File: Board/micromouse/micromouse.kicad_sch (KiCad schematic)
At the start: 51 parts, among them J1 Conn_01x02_Pin, J2 Conn_02x03_Odd_Even, J4 Conn_01x06_Pin, J5 Conn_01x06_Pin, M1 Motor_DC, M2 Motor_DC, Q1 DMN63D8L-7, Q7 GSFC02A05, SW1 AYZ0102AGRLC, SW2 NANOT 100 AS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

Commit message: レビュー対応
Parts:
- D10, D11, D12, D13: footprint LED_SMD:LED_0603_1608Metric -> LED_SMD:LED_0402_1005Metric
- J1: footprint Connector_JST:JST_PH_B2B-PH-SM4-TB_1x02-1MP_P2.00mm_Vertical -> Connector_JST:JST_PH_B2B-PH-K_1x02_P2.00mm_Vertical
- R24, R25, R26, R27, R4: value 1k -> 3.3k
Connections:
- net +3.3V: now also R1.2, R2.2, R33.1; no longer SW4.2
- net GND: now also R23.1, SW4.1; no longer Q7.1 (G), R33.2
- net NRST: now also R33.2, SW4.2; no longer R33.1, SW4.1
- net at R3.2, SW1.1 (A): now also Q7.1 (G)
- no-connect marks 22 -> 19
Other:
- moved on the sheet: R1, R2, R33, SW1

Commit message: ボタン位置修正
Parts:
- D1: footprint LED_SMD:LED_0603_1608Metric -> LED_SMD:LED_0402_1005Metric_Pad0.77x0.64mm_HandSolder
- D10, D11, D12, D13: footprint LED_SMD:LED_0402_1005Metric -> LED_SMD:LED_0402_1005Metric_Pad0.77x0.64mm_HandSolder
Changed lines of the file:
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@@
       (effects (font (size 1.27 1.27)) (justify right))
     )
-    (property "Footprint" "LED_SMD:LED_0603_1608Metric" (at 114.3 31.75 0)
+    (property "Footprint" "LED_SMD:LED_0402_1005Metric_Pad0.77x0.64mm_HandSolder" (at 114.3 31.75 0)
       (effects (font (size 1.27 1.27)) hide)
     )
@@
       (effects (font (size 1.27 1.27)))
     )
-    (property "Footprint" "LED_SMD:LED_0402_1005Metric" (at 267.97 73.66 0)
+    (property "Footprint" "LED_SMD:LED_0402_1005Metric_Pad0.77x0.64mm_HandSolder" (at 267.97 73.66 0)
       (effects (font (size 1.27 1.27)) hide)
     )
@@
       (effects (font (size 1.27 1.27)))
     )
-    (property "Footprint" "LED_SMD:LED_0402_1005Metric" (at 267.97 88.9 0)
+    (property "Footprint" "LED_SMD:LED_0402_1005Metric_Pad0.77x0.64mm_HandSolder" (at 267.97 88.9 0)
       (effects (font (size 1.27 1.27)) hide)
     )
@@
       (effects (font (size 1.27 1.27)))
     )
-    (property "Footprint" "LED_SMD:LED_0402_1005Metric" (at 267.97 96.52 0)
+    (property "Footprint" "LED_SMD:LED_0402_1005Metric_Pad0.77x0.64mm_HandSolder" (at 267.97 96.52 0)
       (effects (font (size 1.27 1.27)) hide)
     )
@@
       (effects (font (size 1.27 1.27)))
     )
-    (property "Footprint" "LED_SMD:LED_0402_1005Metric" (at 267.97 81.28 0)
-      (effects (font (size 1.27 1.27)) hide)
-    )
+    (property "Footprint" "LED_SMD:LED_0402_1005Metric_Pad0.77x0.64mm_HandSolder" (at 267.97 81.28 0)
+      (effects (font (size 1.27 1.27)) hide)
+    )

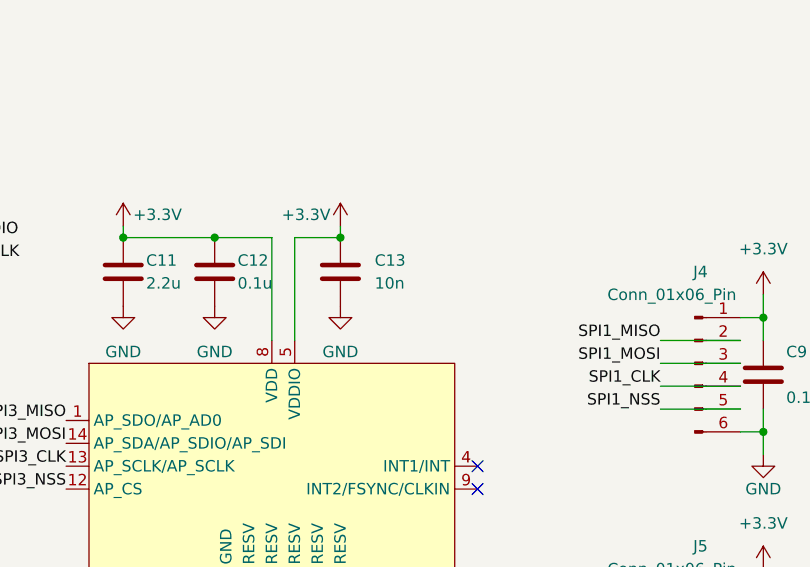
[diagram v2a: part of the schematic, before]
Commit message: 部品型番、URLを追加
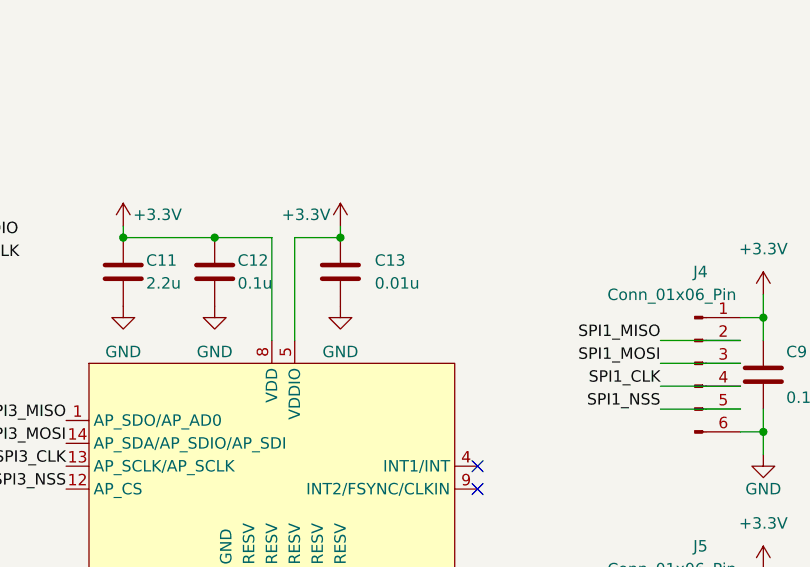
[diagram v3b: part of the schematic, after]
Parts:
- BZ1: manf# (none) -> SMT-0440-T-HT-R
- C1: manf# (none) -> C1206X106K3RACAUTO; order_URL (none) -> https://www.digikey.jp/ja/products/detail/kemet/C1206X106M3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
- C10, C12, C14, C15, C16, C17, C18, C19, C8, C9: manf# (none) -> CGA2B3X5R1H104K050BB; order_URL (none) -> https://www.digikey.jp/ja/products/detail/tdk-corporation/C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
- C11: manf# (none) -> GRT155R61E225KE13D; order_URL (none) -> https://www.digikey.jp/ja/products/detail/murata-electronic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
- C13: value 10n -> 0.01u; manf# (none) -> GCM155R71H103KA55D; order_URL (none) -> https://www.digikey.jp/ja/products/detail/murata-electronic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
- C2, C3: manf# (none) -> GRT155R6YA105KE13D; order_URL (none) -> https://www.digikey.jp/ja/products/detail/murata-electronic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
- D1: manf# (none) -> SML-P12M2TT86R; order_URL https://akizukidenshi.com/catalog/g/gI-08275/ -> https://www.digikey.jp/ja/products/detail/rohm-semiconducto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
- D10, D11, D12, D13: manf# (none) -> SML-P12YTT86R; order_URL (none) -> https://www.digikey.jp/ja/products/detail/rohm-semiconducto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
- D14: manf# (none) -> 1N4448W-TP
- J1: manf# (none) -> B2B-PH-K-S; order_URL (none) -> https://www.digikey.jp/ja/products/detail/jst-sales-america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
- J4, J5, M1, M2: manf# (none) -> -
- R1, R2, R23: manf# (none) -> AC0402JR-070RL; order_URL (none) -> https://www.digikey.jp/ja/products/detail/yageo/AC0402JR-07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
- R21: manf# (none) -> AC0402FR-076K8L; order_URL (none) -> https://www.digikey.jp/ja/products/detail/yageo/AC0402FR-07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
- R22: manf# (none) -> AC0402FR-0715KL; order_URL (none) -> https://www.digikey.jp/ja/products/detail/yageo/AC0402FR-07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
- R24, R25, R26, R27, R4: manf# (none) -> AC0402FR-073K3L; order_URL (none) -> https://www.digikey.jp/ja/products/detail/yageo/AC0402FR-07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
- R28, R33: manf# (none) -> AC0402FR-0710KL; order_URL (none) -> https://www.digikey.jp/ja/products/detail/yageo/AC0402FR-07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
- R3: manf# (none) -> AC0402FR-07100KL; order_URL (none) -> https://www.digikey.jp/ja/products/detail/yageo/AC0402FR-07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
